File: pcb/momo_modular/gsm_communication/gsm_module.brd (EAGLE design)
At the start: 68.6 x 33 mm, 22 parts, among them U1 PIC16LF1823, U2 TI-HIGHSIDE-PFET, U3 SIM900, U4 ESD-SMF05C

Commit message: Fixed C1 wiring to properly do soft-start
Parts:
- moved R5 2.21 mm to (14.5, 16.3), turned to 180 degrees
- moved R2 0.70 mm to (13.7, 20.2), turned to 270 degrees
- moved C3 0.56 mm to (6.86, 7.34), turned to 270 degrees
- moved C1 0.37 mm to (15.3, 18.5), turned to 270 degrees
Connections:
- net N$3: now also C1.2
- net V+: no longer C1.2
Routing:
- net N$3: track 2.35 -> 9.94 mm
- net GND: track 223.1 -> 217.7 mm
- net N$4: track 12.3 -> 8.24 mm
- net POW-SW-ON: track 23.9 -> 24.6 mm
- net V+: track 14.2 -> 14.8 mm

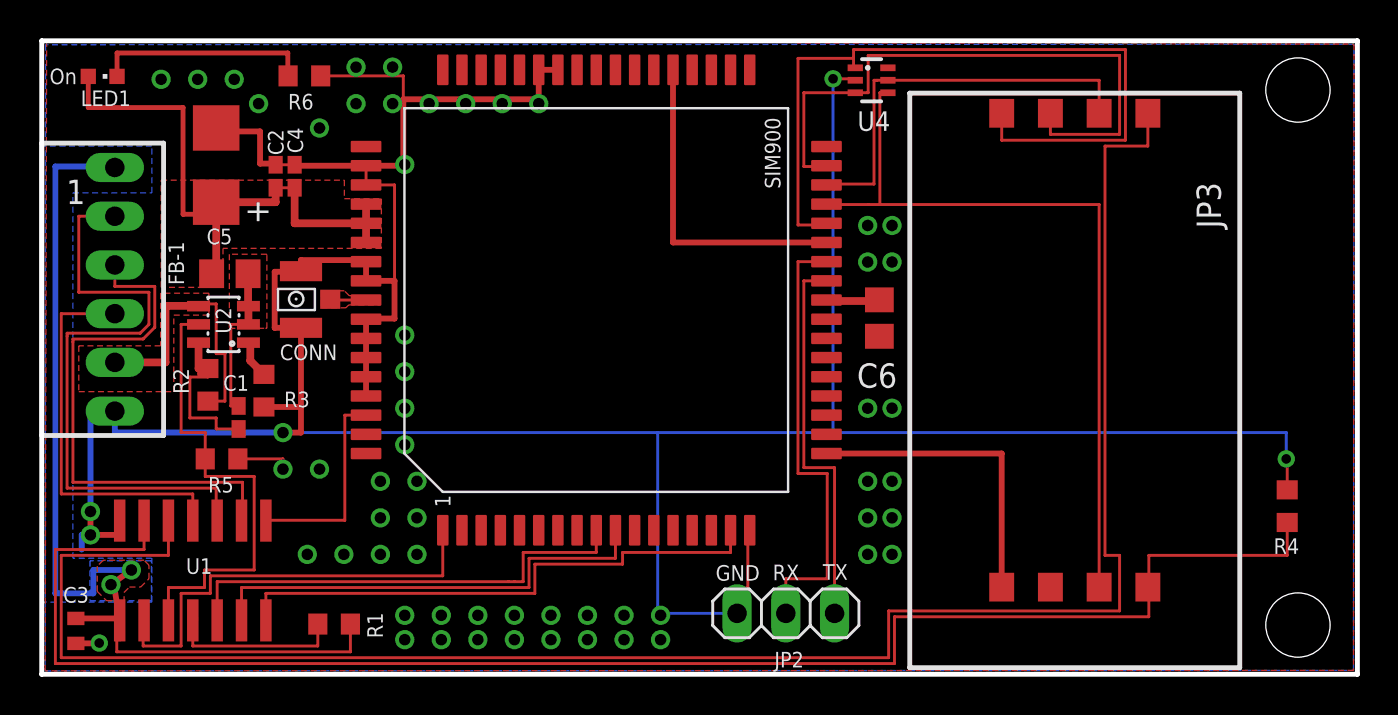
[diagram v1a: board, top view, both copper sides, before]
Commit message: Re-layout gsm_module to use sd/card adapter
Board is now 2" long, fitting a 1M form-factor and allowing the
controller board to be expanded in order to make more space for
power connectors.
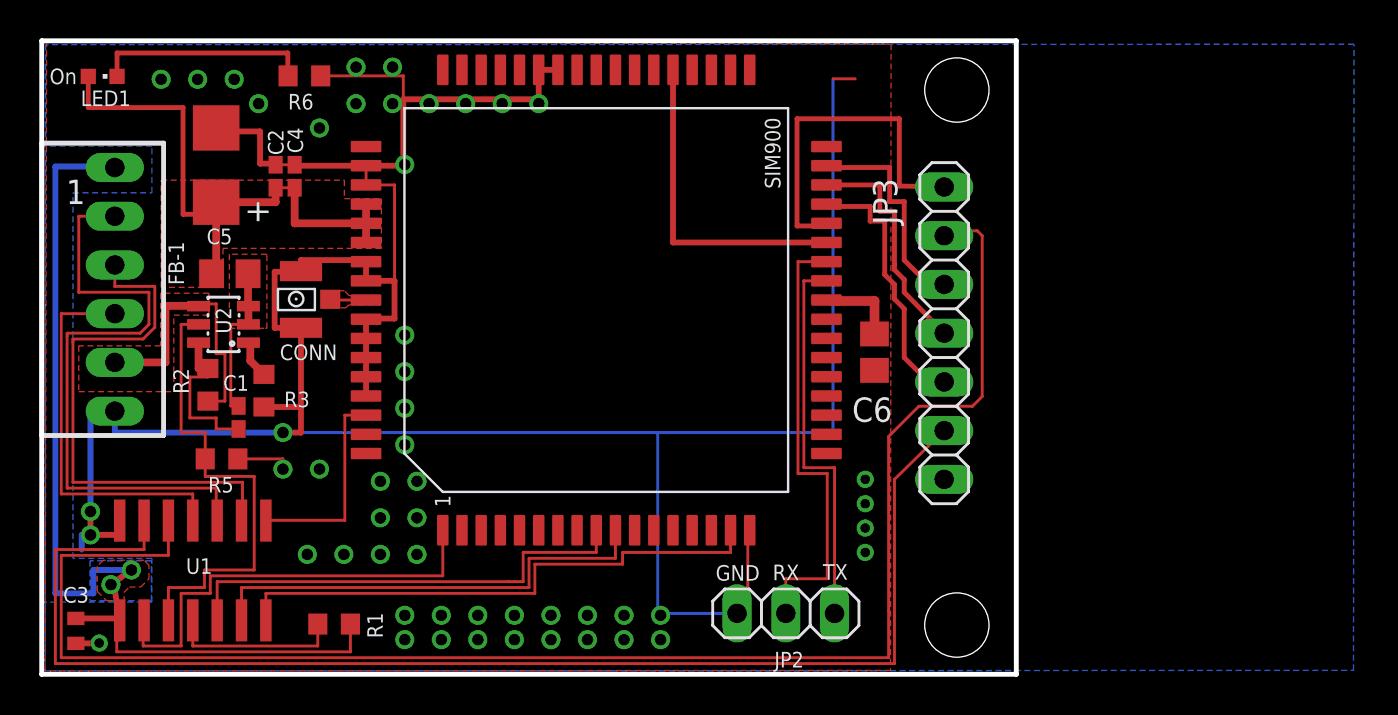
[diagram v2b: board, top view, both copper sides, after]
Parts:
- removed R4: 10K, rcl:R0603
- removed U4: ESD-SMF05C, components:SC70-6L
- JP3: value SIMHOLDER-8PINHING -> (none); device components:CCM03-SIMHOLDER -> pinhead:1X07
- moved JP3 6.87 mm to (52.1, 22.9), turned to 270 degrees
- moved C6 1.80 mm to (48.5, 21.9)
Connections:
- net GND: now also JP3.7; no longer JP3.GND, R4.1, U4.2
- net SIMCLK: now also JP3.4; no longer JP3.CLOCK, U4.5
- net SIMDAT: now also JP3.5; no longer JP3.IO, U4.4
- net SIMRST: now also JP3.3; no longer JP3.RESET, U4.3
- net SIMVCC: now also JP3.1; no longer JP3.VCC, U4.1
- net SW1: now also JP3.2; no longer JP3.SW1
- net SW2: now also JP3.6; no longer JP3.SW2, R4.2
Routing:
- net GND: track 217.7 -> 174.9 mm, vias 62 -> 52
- net SIMDAT: track 40.4 -> 14.0 mm
- net SIMVCC: track 40.9 -> 18.4 mm
- net SIMRST: track 32.3 -> 11.6 mm
- net SW1: track 99.3 -> 83.7 mm
- net SW2: track 83.7 -> 69.0 mm
- net SIMCLK: track 21.4 -> 12.3 mm
- net N$5: track 3.16 -> 4.27 mm
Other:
- board size 68.6 x 33 mm -> 50.8 x 33 mm
